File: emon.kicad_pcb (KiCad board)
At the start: 2 copper layers, 50.8 x 22.9 mm, 12 parts, among them J1 Screw_Terminal_01x02, J2 Conn_01x03_MountingPin, J3 USB_C_Receptacle_PowerOnly_6P, SW1 RESET, SW2 BOOTSEL, U1 RAK3172-T-8-SM-I, U2 BME690, U3 BQ25185

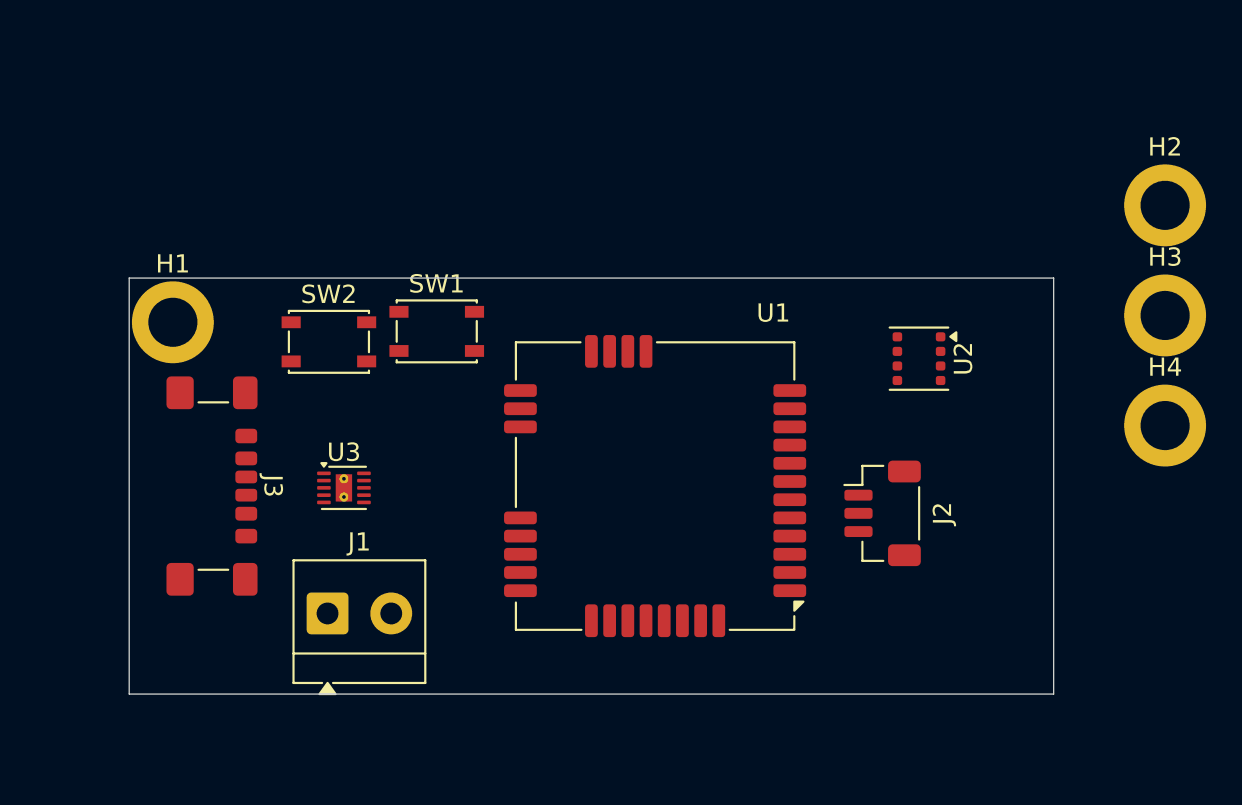
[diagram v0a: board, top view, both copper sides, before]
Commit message: finish schematic, start layout
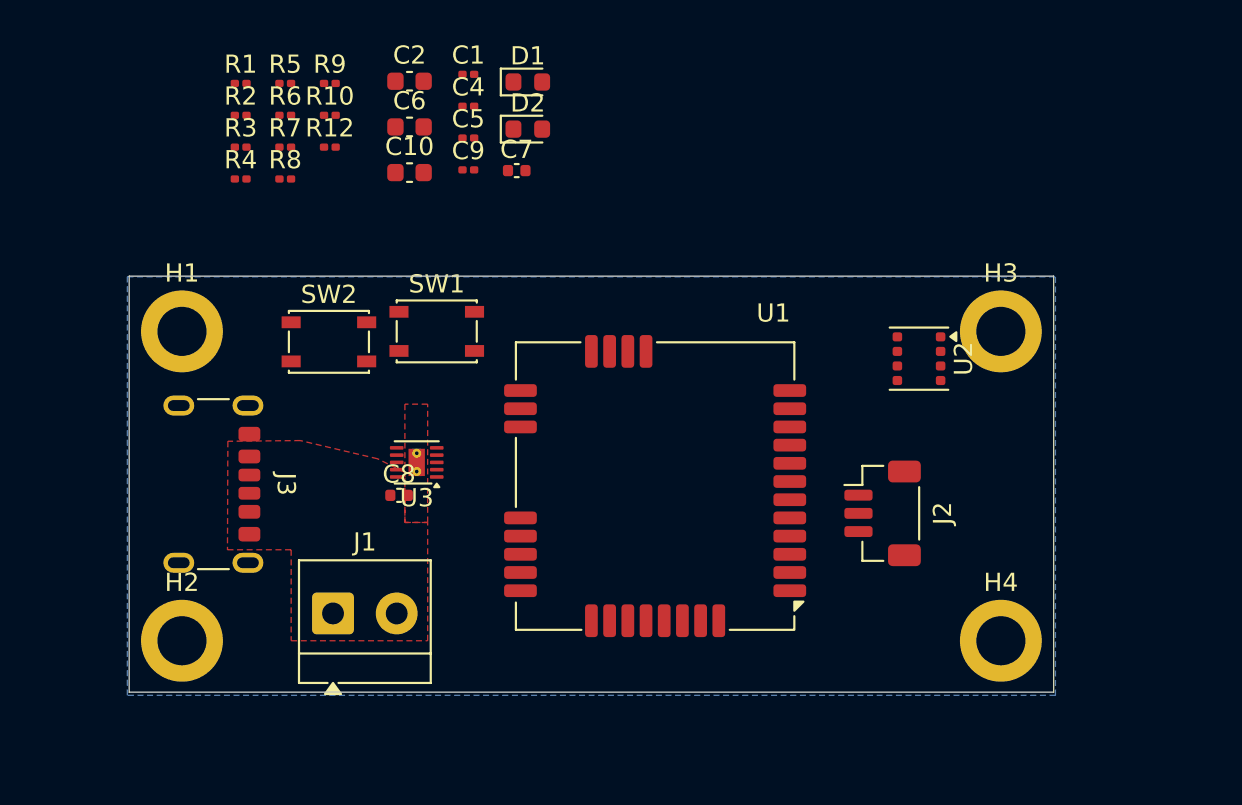
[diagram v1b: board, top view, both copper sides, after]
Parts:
- added C1: 100n, Capacitor_SMD:C_0201_0603Metric, F.Cu at (141.7, 82.4)
- added C10: 10u, Capacitor_SMD:C_0603_1608Metric, F.Cu at (138.5, 87.8)
- added C2: 10u, Capacitor_SMD:C_0603_1608Metric, F.Cu at (138.5, 82.8)
- added C4: 100n, Capacitor_SMD:C_0201_0603Metric, F.Cu at (141.7, 84.1)
- added C5: 100n, Capacitor_SMD:C_0201_0603Metric, F.Cu at (141.7, 85.9)
- added C6: 10u, Capacitor_SMD:C_0603_1608Metric, F.Cu at (138.5, 85.3)
- added C7: 1u, Capacitor_SMD:C_0402_1005Metric, F.Cu at (144.4, 87.7)
- added C8: 1u, Capacitor_SMD:C_0402_1005Metric, F.Cu at (137.9, 105.5)
- added C9: 0.1u, Capacitor_SMD:C_0201_0603Metric, F.Cu at (141.7, 87.6)
- added D1: RED, LED_SMD:LED_0603_1608Metric, F.Cu at (145.0, 82.8)
- added D2: ORANGE, LED_SMD:LED_0603_1608Metric, F.Cu at (145.0, 85.4)
- added R1: 10k, Resistor_SMD:R_0201_0603Metric, F.Cu at (129.2, 82.9)
- added R10: 5.1k, Resistor_SMD:R_0201_0603Metric, F.Cu at (134.1, 84.6)
- added R12: 10k, Resistor_SMD:R_0201_0603Metric, F.Cu at (134.1, 86.4)
- added R2: 4.7k, Resistor_SMD:R_0201_0603Metric, F.Cu at (129.2, 84.6)
- added R3: 4.7k, Resistor_SMD:R_0201_0603Metric, F.Cu at (129.2, 86.4)
- added R4: 10k, Resistor_SMD:R_0201_0603Metric, F.Cu at (129.2, 88.1)
- added R5: 13k, Resistor_SMD:R_0201_0603Metric, F.Cu at (131.7, 82.9)
- added R6: 1k, Resistor_SMD:R_0201_0603Metric, F.Cu at (131.7, 84.6)
- added R7: 10k, Resistor_SMD:R_0201_0603Metric, F.Cu at (131.7, 86.4)
- added R8: 10k, Resistor_SMD:R_0201_0603Metric, F.Cu at (131.7, 88.1)
- added R9: 5.1k, Resistor_SMD:R_0201_0603Metric, F.Cu at (134.1, 82.9)
- H1, H2, H3, H4: footprint MountingHole:MountingHole_2.7mm_M2.5_ISO7380_Pad -> MountingHole:MountingHole_2.7mm_M2.5_ISO14580_Pad
- J3: footprint Connector_USB:USB_C_Receptacle_GCT_USB4135-GF-A_6P_TopMnt_Horizontal -> Connector_USB:USB_C_Receptacle_GCT_USB4125-xx-x_6P_TopMnt_Horizontal
- moved H2 59.1 mm to (126.0, 113.5)
- moved H4 14.9 mm to (171.0, 113.5)
- moved H3 9.07 mm to (171.0, 96.5)
- moved U3 4.24 mm to (138.9, 103.7), turned to 180 degrees
- moved H1 0.71 mm to (126.0, 96.5)
- moved J1 0.30 mm to (134.3, 112.0)
- moved J3 0.16 mm to (126.6, 104.9)
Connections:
- U3 pad 11: (no net) -> GND
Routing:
- added copper zone on B.Cu, net GND
- added copper zone on F.Cu, net GND
- added copper zone on F.Cu, net VBUS

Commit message: layout progress
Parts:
- added C11: 1u, Capacitor_SMD:C_0603_1608Metric_Pad1.08x0.95mm_HandSolder, F.Cu at (153.2, 88.0)
- added C12: 1u, Capacitor_SMD:C_0603_1608Metric_Pad1.08x0.95mm_HandSolder, F.Cu at (153.2, 90.5)
- added J4: Conn_01x02_MountingPin, Connector_JST:JST_PH_S2B-PH-SM4-TB_1x02-1MP_P2.00mm_Horizontal, F.Cu at (131.3, 95.4)
- added U4: AP2112K-3.3, Package_TO_SOT_SMD:SOT-23-5_HandSoldering, F.Cu at (137.9, 105.8)
- C6: footprint Capacitor_SMD:C_0603_1608Metric -> Capacitor_SMD:C_0402_1005Metric
- moved D1 28.9 mm to (136.3, 110.4), turned to 180 degrees
- moved D2 25.0 mm to (136.4, 108.8), turned to 180 degrees
- moved C10 24.6 mm to (128.0, 110.0), turned to 90 degrees
- moved R7 23.6 mm to (134.1, 109.8)
- moved R9 22.6 mm to (127.2, 104.4)
- moved C6 22.3 mm to (132.9, 106.8)
- moved R10 21.9 mm to (127.2, 105.4)
- moved R6 21.1 mm to (129.8, 105.7), turned to 90 degrees
- moved R8 21.0 mm to (134.1, 109.0)
- moved R5 20.7 mm to (129.9, 103.5), turned to -90 degrees
- moved C9 19.8 mm to (129.1, 102.9), turned to -90 degrees
- moved C7 18.9 mm to (133.7, 103.2)
- moved R4 15.0 mm to (131.1, 103.1), turned to -90 degrees
- moved SW2 7.02 mm to (140.1, 93.4), turned to 90 degrees
- moved U3 7.02 mm to (132.0, 105.0)
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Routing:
- net GND: track 0.00 -> 19.6 mm, vias 0 -> 16
- net Net-(U3-STAT1): track 0.00 -> 6.92 mm, vias 0 -> 2
- net Net-(U3-STAT2): track 0.00 -> 6.84 mm, vias 0 -> 2
- net /BOOT: track 0.00 -> 4.95 mm
- net /RST: track 0.00 -> 4.15 mm
- net Net-(J3-CC2): track 0.00 -> 1.76 mm
- net Net-(J3-CC1): track 0.00 -> 1.76 mm
- net /ILIM/VSET: track 0.00 -> 1.52 mm
- net /ISET: track 0.00 -> 1.38 mm
- net Net-(D1-A): track 0.00 -> 1.32 mm
- net Net-(D2-A): track 0.00 -> 1.18 mm
- net /TS/MR: track 0.00 -> 0.91 mm
- added copper zone on F.Cu, net +3V3
- added copper zone on F.Cu, net +BATT
- added copper zone on F.Cu, net VDD
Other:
- board size 50.8 x 22.9 mm -> 60 x 30 mm
